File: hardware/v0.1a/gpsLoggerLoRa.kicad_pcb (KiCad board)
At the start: 4 copper layers, 41 x 72.8 mm, 86 parts, among them P1 USB_OTG, P2 CONN_01X02, SW1 SW_PUSH, U2 MCP73812, U6 TPS78230, U8 ATSAMR34J18B, U9 PE4259

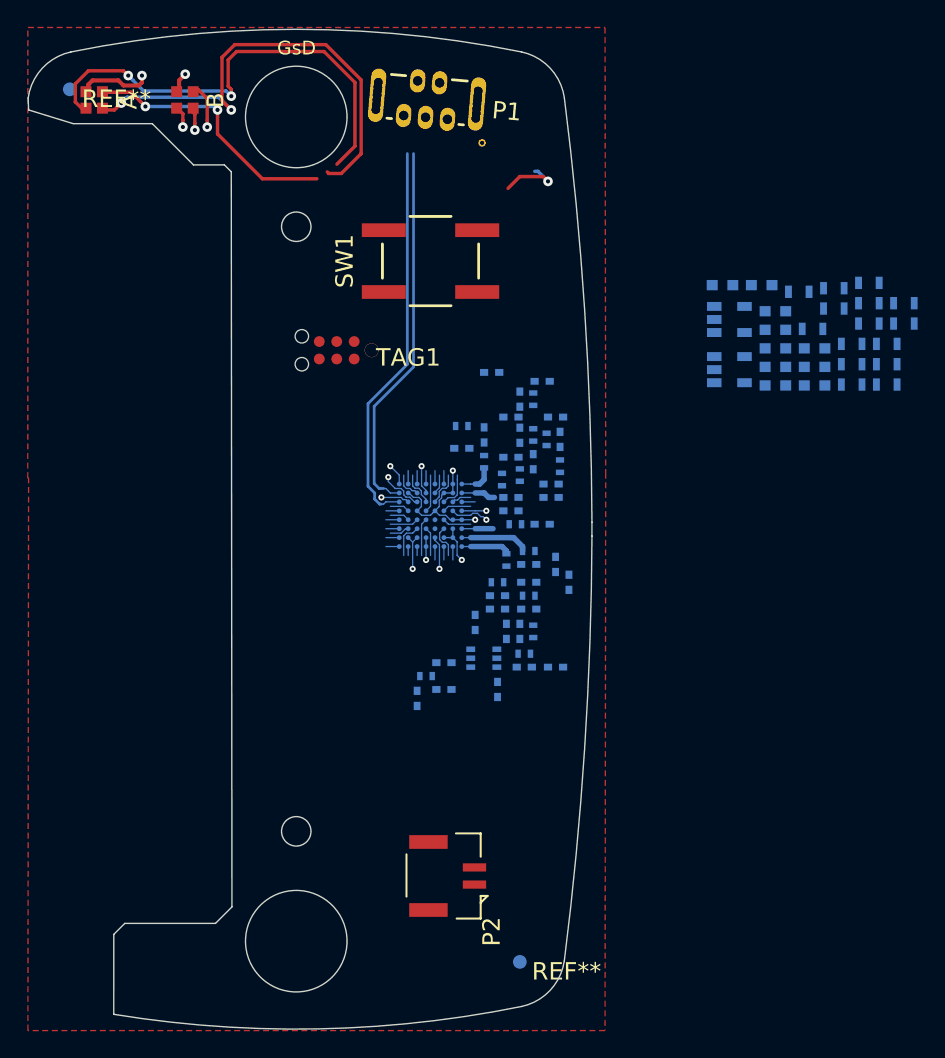
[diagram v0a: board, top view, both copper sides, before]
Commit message: Changed USB connector. Updated board outline. Updates to footprints to use 3d models. Add FLASH memory.
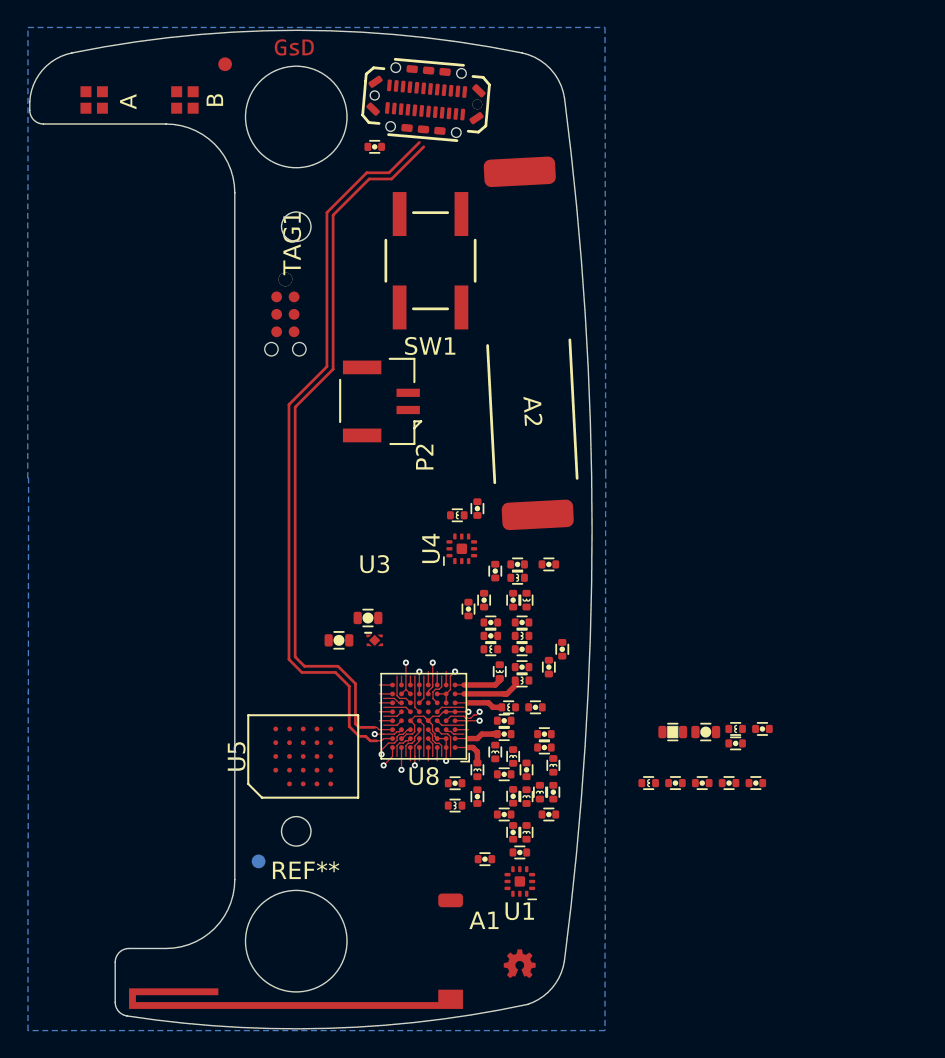
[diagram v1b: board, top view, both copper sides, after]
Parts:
- removed C30, C32: 18pF, Capacitors_SMD:C_0402_NoSilk
- removed FB1: 1k FB, Resistors_SMD:R_0603
- removed P1: USB_OTG, footprints:USB_VERT
- removed R10, R16, R17, R18, R19, R20, R21, R7: 1k, Resistors_SMD:R_0603
- removed R12, R15: 10k, Resistors_SMD:R_0603
- removed R13, R14: 100k, Resistors_SMD:R_0603
- removed R2: 27R, Resistors_SMD:R_0603
- removed the REF** at (165.0, 74.4)
- removed U2: MCP73812, TO_SOT_Packages_SMD:SOT-23-5
- removed U6: TPS78230, TO_SOT_Packages_SMD:SOT-23-5
- removed U9: PE4259, TO_SOT_Packages_SMD:SOT-363_SC-70-6
- added A1: pkl_ANTENNA, gkl_antenna:0900AT43A0070 - 900MHz Wide band ISM Chip Antenna, F.Cu at (162.7, 133.0)
- added A2: pkl_ANTENNA, gkl_antenna:0433AT62A0020 - 433MHz 25x5x1mm chip antenna, F.Cu at (168.4, 89.0)
- added G***: LOGO, gkl_logos:gsd_logo_small, F.Cu at (151.3, 67.5)
- added G***: LOGO, gkl_logos:oshw_small, F.Cu at (167.8, 134.2)
- added J1: USB_C_Receptacle, gkl_conn:usbc_vert_10132328, F.Cu at (160.9, 71.3)
- added L17: 1k, pkl_dipol:L_0402, F.Cu at (183.5, 117.1)
- added L18: 1k, pkl_dipol:L_0402, F.Cu at (177.1, 121.0)
- added U1: SKY13373, gkl_housings_qfn:QFN-12-1EP_3x3mm_P0.5mm_EP1.65x1.65mm, F.Cu at (167.8, 128.2)
- added U3: NCP167, gkl_housings_son:X2SON_4_1.0x1.0mm, F.Cu at (157.2, 110.6)
- added U4: SKY13373, gkl_housings_qfn:QFN-12-1EP_3x3mm_P0.5mm_EP1.65x1.65mm, F.Cu at (163.5, 103.9)
- added U5: MT25QL256ABA8E12, gkl_housings_bga:T-PBGA-24_6.0x8.0mm_Layout5x5_P1.0mm, F.Cu at (152.0, 119.0)
- C1: value 10n -> 100nF; footprint Capacitors_SMD:C_0603 -> pkl_dipol:C_0402; moved to F.Cu
- C10, C12, C13, C18, C19, C20, C21, C22, C23, C24, C25, C26, C27, C28, C29, C31, C33, C34, C35, C36, C37, C38, C39, C4, C40, C41, C42, C5, C7, C8: footprint Capacitors_SMD:C_0402_NoSilk -> pkl_dipol:C_0402; moved to F.Cu
- C11, C6: value 100n -> 100nF; footprint Capacitors_SMD:C_0603 -> pkl_dipol:C_0402; moved to F.Cu
- C14: value 100n -> 1uF; footprint Capacitors_SMD:C_0603 -> pkl_dipol:C_0603; moved to F.Cu
- C15: value 1uF -> 100nF; footprint Capacitors_SMD:C_0603 -> pkl_dipol:C_0402; moved to F.Cu
- C16, C17: footprint Capacitors_SMD:C_0603 -> pkl_dipol:C_0603; moved to F.Cu
- C2, C3: value 22p -> 100nF; footprint Capacitors_SMD:C_0603 -> pkl_dipol:C_0402; moved to F.Cu
- C9: value 100n -> 10n; footprint Capacitors_SMD:C_0603 -> pkl_dipol:C_0402; moved to F.Cu
- L1, L10, L11, L12, L13, L14, L15, L16, L2, L3, L4, L5, L6, L7, L8, L9: footprint Inductors_SMD:L_0402 -> pkl_dipol:L_0402; moved to F.Cu
- R1: value 27R -> R; footprint Resistors_SMD:R_0603 -> pkl_dipol:R_0603; moved to F.Cu
- REF**: moved to B.Cu
- U8: footprint Package_BGA:XFBGA-64_5.0x5.0mm_Layout8x8_P0.5mm -> gkl_housings_bga:TFBGA-64_6.0x6.0mm_Layout8x8_P0.65mm; moved to F.Cu
- moved C17 39.8 mm to (154.6, 110.6)
- moved C14 36.3 mm to (156.7, 109.0)
- moved C3 36.3 mm to (181.0, 121.0)
- moved R1 35.5 mm to (178.9, 117.3)
- moved C42 35.4 mm to (165.2, 126.5)
- moved P2 34.9 mm to (159.6, 93.2)
- moved C41 34.3 mm to (167.8, 126.0), turned to 0 degrees
- moved C16 32.8 mm to (181.3, 117.3)
- moved C11 32.6 mm to (157.2, 74.7)
- moved C2 32.2 mm to (183.0, 121.0)
- moved C39 31.5 mm to (167.3, 124.6), turned to 270 degrees
- moved L16 31.5 mm to (168.2, 124.6), turned to 270 degrees
- moved C6 30.7 mm to (179.1, 121.0)
- moved C1 29.0 mm to (184.9, 121.0)
- moved C37 28.9 mm to (166.6, 123.3)
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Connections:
- net VDDA renamed AVDD
- C1 pad 1: Net-(C1-Pad1) -> GND
- C1 pad 2: GND -> Net-(C1-Pad2)
- C11 pad 1: PWR_BUT -> Net-(C11-Pad1)
- C14 pad 1: +BATT -> Net-(C11-Pad1)
- C15 pad 1: +3V3 -> Net-(C15-Pad1)
- C16 pad 1: 1v8 -> Net-(C15-Pad1)
- C17 pad 1: VUSB -> +3V3
- C2 pad 1: /USB_DATA_N -> GND
- C2 pad 2: GND -> +3V3
- C3 pad 1: /USB_DATA_P -> GND
- C3 pad 2: GND -> +3V3
- C6 pad 1: /VBUS -> GND
- C6 pad 2: GND -> +3V3
- C9 pad 1: +BATT -> Net-(C9-Pad1)
- L4 pad 1: Net-(C12-Pad1) -> /SAMR34/VR_PA
- L4 pad 2: /SAMR34/VR_PA -> Net-(C12-Pad1)
- R1 pad 1: /USB_DATA_N -> Net-(R1-Pad1)
- R1 pad 2: /USB_IN_N -> GND
- U8 pad A7: Net-(U8-PadA7) -> +3V3
- U8 pad A8: Net-(U8-PadA8) -> +3V3
- U8 pad B8: /USB_DATA_N -> /SAMR34/USB_DATA_N
- U8 pad C2: Net-(U8-PadC2) -> Net-(C1-Pad2)
- U8 pad C8: /USB_DATA_P -> /SAMR34/USB_DATA_P
- U8 pad G4: Net-(U8-PadA8) -> +3V3
- U8 pad G8: Net-(U8-PadG8) -> /SAMR34/SHDN
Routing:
- net /SAMR34/USB_DATA_N: track 0.00 -> 54.3 mm
- net /SAMR34/USB_DATA_P: track 0.00 -> 52.9 mm
- net Net-(D1-Pad4): track 49.6 -> 0.00 mm, vias 2 -> 0
- net Net-(D1-Pad3): track 48.3 -> 0.00 mm, vias 2 -> 0
- net +3V3: track 40.6 -> 5.60 mm, vias 2 -> 3
- net Net-(D1-Pad2): track 32.4 -> 0.00 mm, vias 2 -> 0
- net Net-(D2-Pad4): track 29.4 -> 0.00 mm, vias 1 -> 0
- net Net-(D2-Pad2): track 28.8 -> 0.00 mm, vias 1 -> 0
- net /USB_DATA_P: track 28.5 -> 0.00 mm
- net Net-(D2-Pad3): track 28.1 -> 0.00 mm, vias 1 -> 0
- net /USB_DATA_N: track 27.3 -> 0.00 mm
- net /TEST: track 11.3 -> 0.00 mm
- net GND: track 30.7 -> 20.5 mm, vias 7 -> 6
- net /RST: track 9.79 -> 0.00 mm
- net Net-(U8-PadA8): track 3.98 -> 0.00 mm, vias 2 -> 0
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- added copper zone on B.Cu, net GND
- removed copper zone on F.Cu, net GND
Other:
- board size 41 x 72.8 mm -> 40.9 x 72.7 mm
- board text removed: "GsD"

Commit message: First pass schematic done. Begin routing main board.
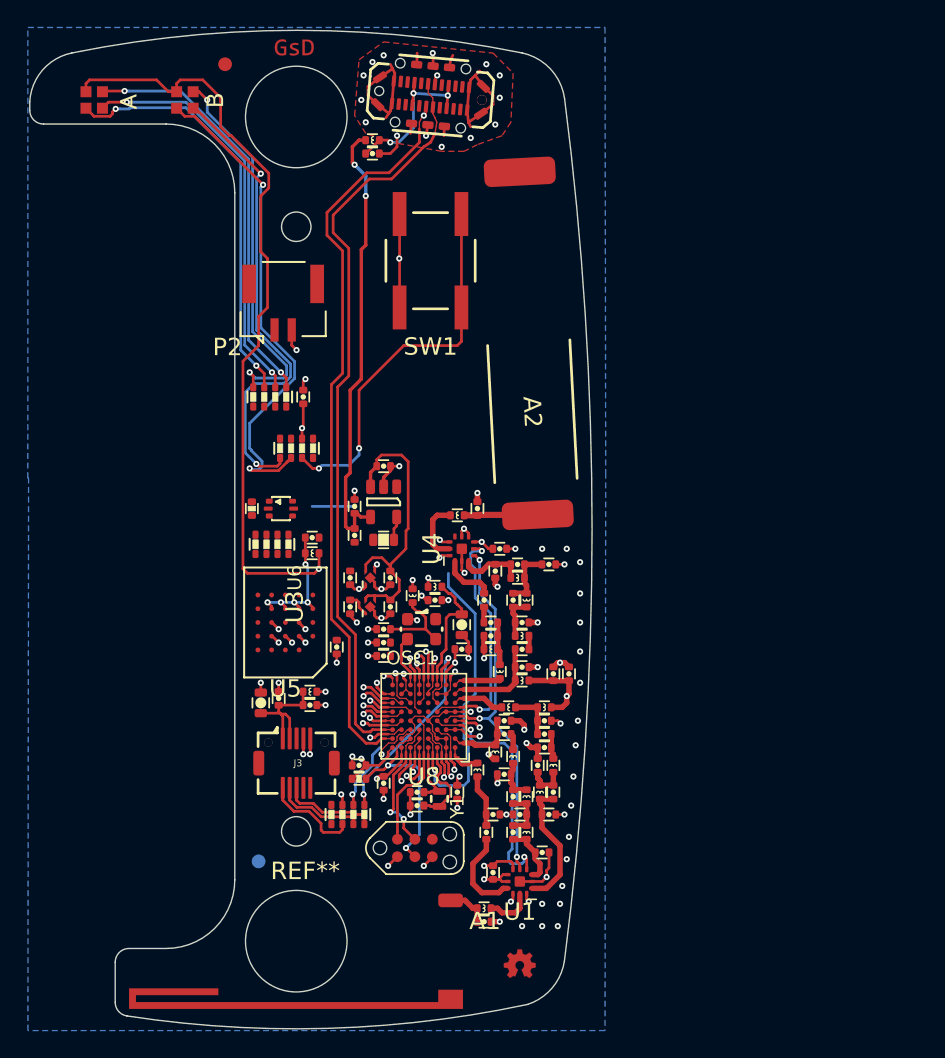
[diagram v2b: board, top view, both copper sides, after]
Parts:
- removed TAG1: TAG_CONNECT, lib:tag_connect
- added C30: 33nF, pkl_dipol:C_0402, F.Cu at (163.5, 111.2)
- added C32: 100nF, pkl_dipol:C_0402, F.Cu at (161.6, 107.7)
- added C43: 100nF, pkl_dipol:C_0402, F.Cu at (152.6, 103.1)
- added C44: 100nF, pkl_dipol:C_0402, F.Cu at (154.4, 111.1)
- added C45: 10uF, pkl_dipol:C_0603, F.Cu at (163.5, 109.5)
- added C46: 10uF, pkl_dipol:C_0603, F.Cu at (148.9, 115.2)
- added C47: 100nF, pkl_dipol:C_0402, F.Cu at (157.8, 111.7)
- added C48: 100nF, pkl_dipol:C_0402, F.Cu at (157.8, 109.8)
- added C49: 10pF, pkl_dipol:C_0402, F.Cu at (160.3, 121.7)
- added C50: 10pF, pkl_dipol:C_0402, F.Cu at (160.3, 122.6)
- added C51: 18pF, pkl_dipol:C_0402, F.Cu at (165.2, 131.1)
- added C52: 100nF, pkl_dipol:C_0402, F.Cu at (158.3, 108.2)
- added C53: 1uF, pkl_dipol:C_0402, F.Cu at (155.4, 106.0)
- added C54: 100nF, pkl_dipol:C_0402, F.Cu at (150.2, 114.8)
- added C55: 100nF, pkl_dipol:C_0402, F.Cu at (152.5, 115.3)
- added C56: 100nF, pkl_dipol:C_0402, F.Cu at (152.0, 92.9)
- added J3: DF12 - 10P, gkl_conn:DF12(3.0)-10DP-0.5V(86), F.Cu at (151.5, 119.5)
- added J4: CTX TAG Connect, pkl_tag_connect:TC2030-NL_SMALL, F.Cu at (160.1, 125.7)
- added L19: 1k, pkl_dipol:L_0402, F.Cu at (152.6, 104.3)
- added L20: 1k, pkl_dipol:L_0402, F.Cu at (152.5, 114.3)
- added L21: 1k, pkl_dipol:L_0402, F.Cu at (159.9, 107.3)
- added L22: 2.2nH, pkl_dipol:L_0402, F.Cu at (165.2, 130.1)
- added OSC1: TYETBCSANF-32.000000, gkl_time:Oscilator_2.5x2.0, F.Cu at (160.6, 109.8)
- added Q1: FG6943010R, pkl_housings_sot:SOT-666, F.Cu at (150.4, 101.0)
- added R2: 100R, pkl_dipol:R_Array_Concave_4x0603, F.Cu at (151.5, 96.6)
- added R3: 100R, pkl_dipol:R_Array_Concave_4x0603, F.Cu at (149.6, 92.9)
- added R4: 100R, pkl_dipol:R_Array_Concave_4x0603, F.Cu at (155.2, 123.3)
- added R5: 10k, pkl_dipol:R_0402, F.Cu at (148.2, 101.0)
- added R6: 47k, pkl_dipol:R_Array_Concave_4x0603, F.Cu at (149.7, 103.6)
- added R7: 10k, pkl_dipol:R_0402, F.Cu at (156.1, 120.7)
- added U2: MCP73832, pkl_housings_sot:SOT-23-5, F.Cu at (157.8, 100.5)
- added U6: NCP167, gkl_housings_son:X2SON_4_1.0x1.0mm, F.Cu at (156.9, 106.0)
- added Y1: 32.768kHz, gkl_time:ABS05_32.768KHz Crystal, F.Cu at (161.9, 122.1)
- C14, C16, C17: footprint pkl_dipol:C_0603 -> pkl_dipol:C_0402
- D1, D2: value Led_RGB_CA -> LED_ARGB
- R1: value R -> 1k
- SW1: value SW_PUSH -> SW_Push
- moved C9 50.4 mm to (157.0, 75.2)
- moved L17 50.3 mm to (157.0, 74.2)
- moved C16 30.4 mm to (157.8, 97.9)
- moved C15 29.2 mm to (158.3, 106.0), turned to 270 degrees
- moved C2 27.0 mm to (156.1, 119.7)
- moved C11 26.2 mm to (155.7, 100.8), turned to 90 degrees
- moved R1 25.3 mm to (157.8, 103.3), turned to 180 degrees
- moved C6 23.6 mm to (157.8, 110.8)
- moved C3 23.2 mm to (157.8, 121.0), turned to 90 degrees
- moved C1 21.7 mm to (163.2, 121.7), turned to 90 degrees
- moved L18 21.1 mm to (161.6, 106.7), turned to 180 degrees
- moved P2 10.5 mm to (150.5, 88.0), turned to 180 degrees
- moved U5 9.84 mm to (150.7, 109.3), turned to 180 degrees
- moved L4 9.66 mm to (169.5, 115.5)
- moved C14 6.09 mm to (155.7, 103.0), turned to 270 degrees
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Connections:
- C1 pad 2: Net-(C1-Pad2) -> AVDD
- D1 pad 1: +3V3 -> /SAMR34/PP3V3_AUX
- D2 pad 1: +3V3 -> /SAMR34/PP3V3_AUX
- L18 pad 1: Net-(C1-Pad2) -> AVDD
- U1 pad 11: Net-(A1-Pad1) -> Net-(L22-Pad1)
- U5 pad A4: Net-(U5-PadA4) -> Net-(C43-Pad1)
- U5 pad B2: Net-(U5-PadB2) -> /SAMR34/FLASH_CLK
- U5 pad B4: +3V3 -> Net-(C43-Pad1)
- U5 pad C2: Net-(U5-PadC2) -> /SAMR34/FLASH_CS#
- U5 pad C4: Net-(U5-PadC4) -> Net-(C43-Pad1)
- U5 pad D2: Net-(U5-PadD2) -> /memio/DQ1
- U5 pad D3: Net-(U5-PadD3) -> /memio/DQ0
- U5 pad D4: Net-(U5-PadD4) -> Net-(C43-Pad1)
- U8 pad B4: Net-(U8-PadB4) -> /SAMR34/LED_B_BLUE
- U8 pad B6: Net-(U8-PadB6) -> /SAMR34/RESET
- U8 pad C1: Net-(U8-PadC1) -> AVDD
- U8 pad C2: Net-(C1-Pad2) -> AVDD
- U8 pad C3: Net-(U8-PadC3) -> /SAMR34/BATTERY_VOLTAGE
- U8 pad C4: Net-(U8-PadC4) -> /SAMR34/AUX_PWR_EN
- U8 pad C5: Net-(U8-PadC5) -> /SAMR34/CLK
- U8 pad C6: Net-(U8-PadC6) -> /USB/CHARGE_STAT
- U8 pad C7: Net-(U8-PadC7) -> /SAMR34/LED_B_GREEN
- U8 pad D3: Net-(U8-PadD3) -> /SAMR34/BAND_SEL
- U8 pad D5: Net-(U8-PadD5) -> /SAMR34/DIO
- U8 pad D7: Net-(U8-PadD7) -> /SAMR34/GPS_RX
- U8 pad D8: Net-(U8-PadD8) -> /SAMR34/GPS_TX
- U8 pad E3: Net-(U8-PadE3) -> /SAMR34/SHDN
- U8 pad E5: Net-(U8-PadE5) -> /SAMR34/LED_B_RED
- U8 pad E6: Net-(U8-PadE6) -> /memio/DQ0
- U8 pad E7: Net-(U8-PadE7) -> /memio/DQ1
- U8 pad E8: Net-(U8-PadE8) -> /SAMR34/FLASH_CLK
- U8 pad F3: Net-(U8-PadF3) -> /SAMR34/LED_A_GREEN
- U8 pad F5: Net-(U8-PadF5) -> /SAMR34/USER_BUTTON
- U8 pad F6: /SAMR34/BAND_SEL -> /SAMR34/LED_A_RED
- U8 pad F7: Net-(U8-PadF7) -> /SAMR34/FLASH_CS#
- U8 pad F8: Net-(U8-PadF8) -> /SAMR34/GPS_PPS
- U8 pad G8: /SAMR34/SHDN -> /SAMR34/LED_A_BLUE
- U8 pad H3: Net-(U8-PadH3) -> AVDD
- U8 pad H8: Net-(U8-PadH8) -> +3V3
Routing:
- net GND: track 20.5 -> 109.5 mm, vias 6 -> 88
- net /SAMR34/PP3V3_AUX: track 0.00 -> 63.1 mm, vias 0 -> 4
- net AVDD: track 0.00 -> 55.5 mm, vias 0 -> 4
- net Net-(D2-Pad4): track 0.00 -> 36.4 mm, vias 0 -> 2
- net Net-(D2-Pad3): track 0.00 -> 34.4 mm, vias 0 -> 2
- net Net-(C11-Pad1): track 0.00 -> 32.9 mm, vias 0 -> 2
- net Net-(D1-Pad4): track 0.00 -> 30.6 mm, vias 0 -> 2
- net Net-(D1-Pad2): track 0.00 -> 30.5 mm, vias 0 -> 2
- net Net-(D1-Pad3): track 0.00 -> 29.7 mm, vias 0 -> 2
- net Net-(D2-Pad2): track 0.00 -> 27.8 mm, vias 0 -> 2
- net Net-(R2-Pad5): track 0.00 -> 27.8 mm, vias 0 -> 2
- net /SAMR34/RX\TX: track 2.83 -> 27.9 mm, vias 1 -> 3
- net /SAMR34/LED_B_BLUE: track 0.00 -> 22.4 mm, vias 0 -> 1
- net Net-(C15-Pad1): track 0.00 -> 21.4 mm
- net /SAMR34/GPS_PPS: track 0.00 -> 19.8 mm, vias 0 -> 3
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- added copper zone on F.Cu, net GND
- added copper zone on In1.Cu, net GND
- removed copper zone on In2.Cu, net GND

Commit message: First pass routing complete.
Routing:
- net /SAMR34/BATTERY_VOLTAGE: track 4.02 -> 50.9 mm, vias 1 -> 7
- net /SAMR34/AUX_PWR_EN: track 4.66 -> 45.4 mm, vias 2 -> 4
- net /USB/CHARGE_STAT: track 3.18 -> 38.2 mm, vias 1 -> 6
- net /SAMR34/LED_B_GREEN: track 2.51 -> 37.0 mm, vias 1 -> 2
- net /SAMR34/LED_A_GREEN: track 0.00 -> 32.6 mm, vias 0 -> 2
- net /SAMR34/USER_BUTTON: track 6.51 -> 35.0 mm, vias 2 -> 3
- net /SAMR34/LED_A_RED: track 2.88 -> 30.7 mm, vias 1 -> 2
- net /SAMR34/LED_B_RED: track 4.17 -> 31.1 mm, vias 1 -> 2
- net /SAMR34/LED_B_BLUE: track 22.4 -> 49.1 mm, vias 1 -> 2
- net /SAMR34/LED_A_BLUE: track 1.66 -> 28.3 mm, vias 1 -> 2
- net +3V3: track 22.3 -> 47.2 mm, vias 6 -> 8
- net Net-(C15-Pad1): track 21.4 -> 35.6 mm, vias 0 -> 2
- net /SAMR34/PP3V3_AUX: track 63.1 -> 74.7 mm
- net /memio/DQ0: track 3.98 -> 13.2 mm
- net /memio/DQ1: track 3.85 -> 13.0 mm
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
